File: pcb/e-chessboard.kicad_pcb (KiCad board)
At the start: 4 copper layers, 170 x 170 mm, 66 parts, among them J1 POWER, J2 UART, Q1 BC847, Q2 BC847, SW1 Reset, SW2 Boot, U1 ESP32-WROOM-32U, U10 MAGNET_LDR, U11 MAGNET_LDR, U12 MAGNET_LDR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

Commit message: feat(kicad): positioning power circuit and uart
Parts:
- U1: moved to B.Cu
- moved U1 247.4 mm to (229.5, 142.0), turned to 90 degrees
- moved R2 158.2 mm to (232.9, 166.5)
- moved R6 153.6 mm to (237.9, 170.0)
- moved R5 146.9 mm to (238.0, 163.5)
- moved U2 138.9 mm to (229.5, 100.5)
- moved C6 134.0 mm to (229.5, 94.5), turned to 180 degrees
- moved C8 129.2 mm to (231.5, 110.5), turned to 180 degrees
- moved F1 127.7 mm to (232.5, 120.0)
- moved D2 126.4 mm to (314.1, 201.1)
- moved D4 126.4 mm to (286.8, 233.5)
- moved D6 126.4 mm to (309.9, 201.1)
- moved D7 126.4 mm to (315.8, 196.8)
- moved R8 126.4 mm to (295.3, 216.8)
- moved C12 126.4 mm to (330.9, 175.5)
- moved C13 126.4 mm to (262.4, 244.6)
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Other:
- board size 170 x 170 mm -> 220 x 170 mm

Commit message: feat(kicad): placing all components
Placing all components to their places.
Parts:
- C3, C4, D1, D2, D4, D5, D6, D7: moved to B.Cu
- moved C14 279.9 mm to (53.0, 137.0), turned to 90 degrees
- moved R7 270.0 mm to (85.0, 66.5), turned to 270 degrees
- moved C15 261.6 mm to (67.0, 133.0), turned to 90 degrees
- moved R8 233.0 mm to (85.0, 116.5), turned to 270 degrees
- moved R9 198.3 mm to (85.0, 166.5), turned to 90 degrees
- moved C12 198.3 mm to (137.0, 217.0), turned to 180 degrees
- moved D9 197.7 mm to (110.0, 85.0), turned to 90 degrees
- moved D10 193.8 mm to (110.0, 135.0), turned to 90 degrees
- moved D11 184.6 mm to (110.0, 185.0), turned to 90 degrees
- moved D12 159.6 mm to (160.0, 85.0), turned to 90 degrees
- moved C13 136.0 mm to (133.0, 203.0), turned to 180 degrees
- moved U13 135.8 mm to (60.0, 135.0)
- moved D13 128.3 mm to (160.0, 135.0), turned to 90 degrees
- moved D14 127.1 mm to (160.2, 185.0), turned to 90 degrees
- moved C3 108.3 mm to (227.0, 128.8)
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
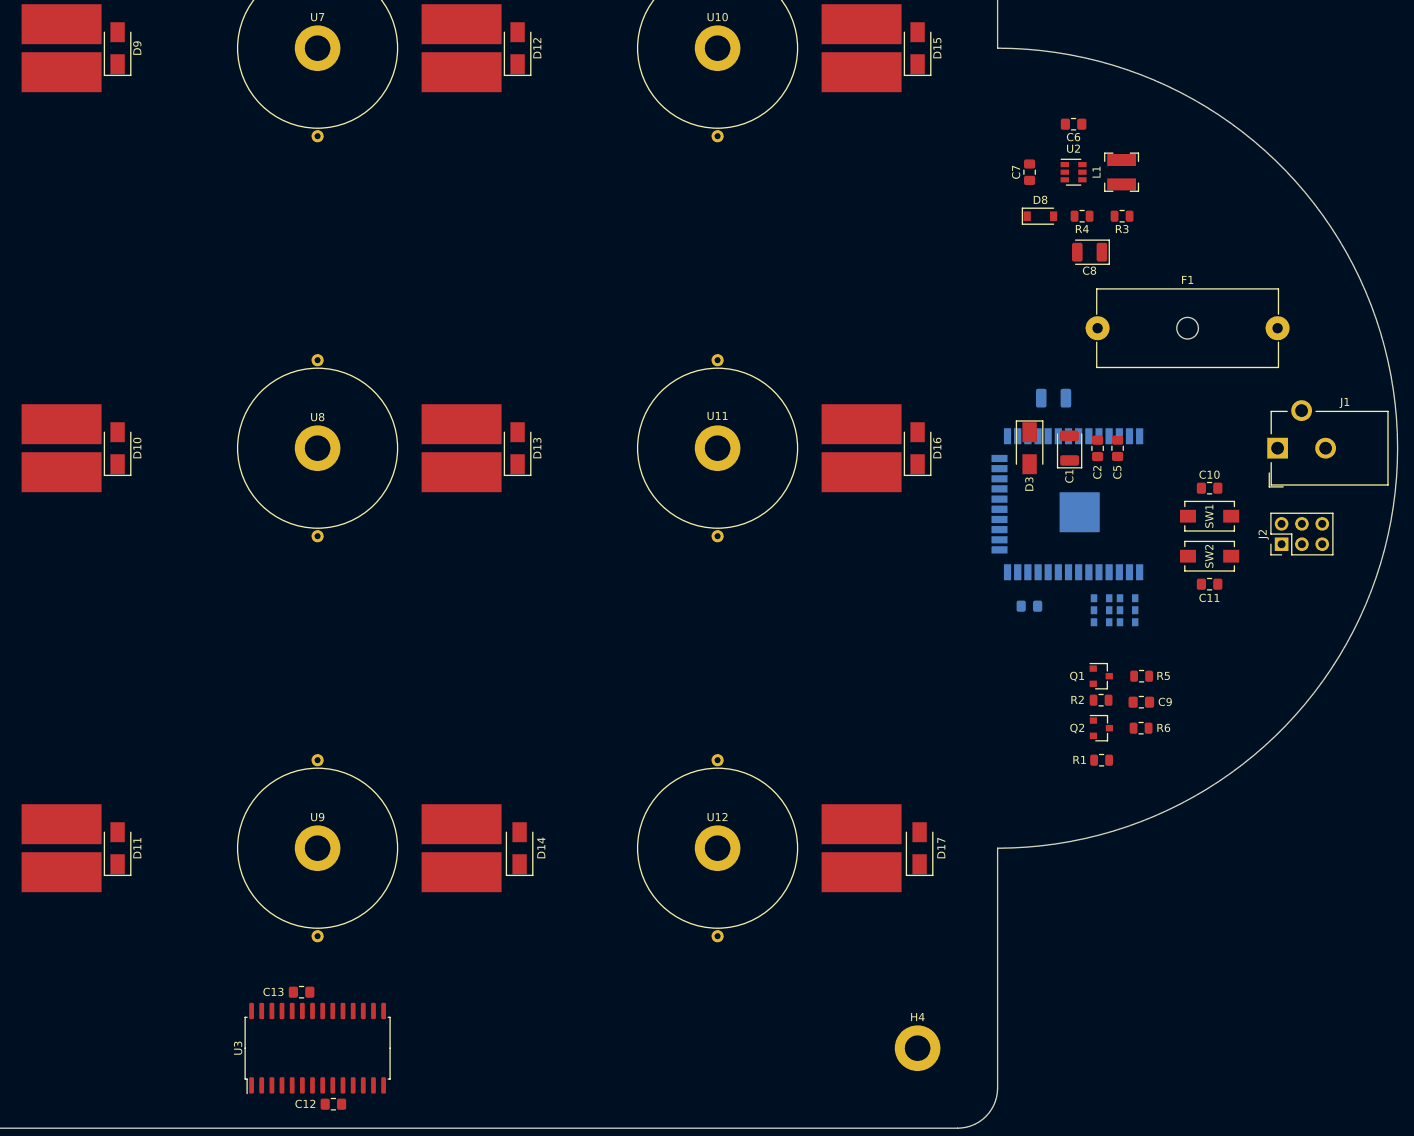
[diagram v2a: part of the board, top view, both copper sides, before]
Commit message: fix(kicad): redesign pcb
Removing outlayer to decrease the pcb size.
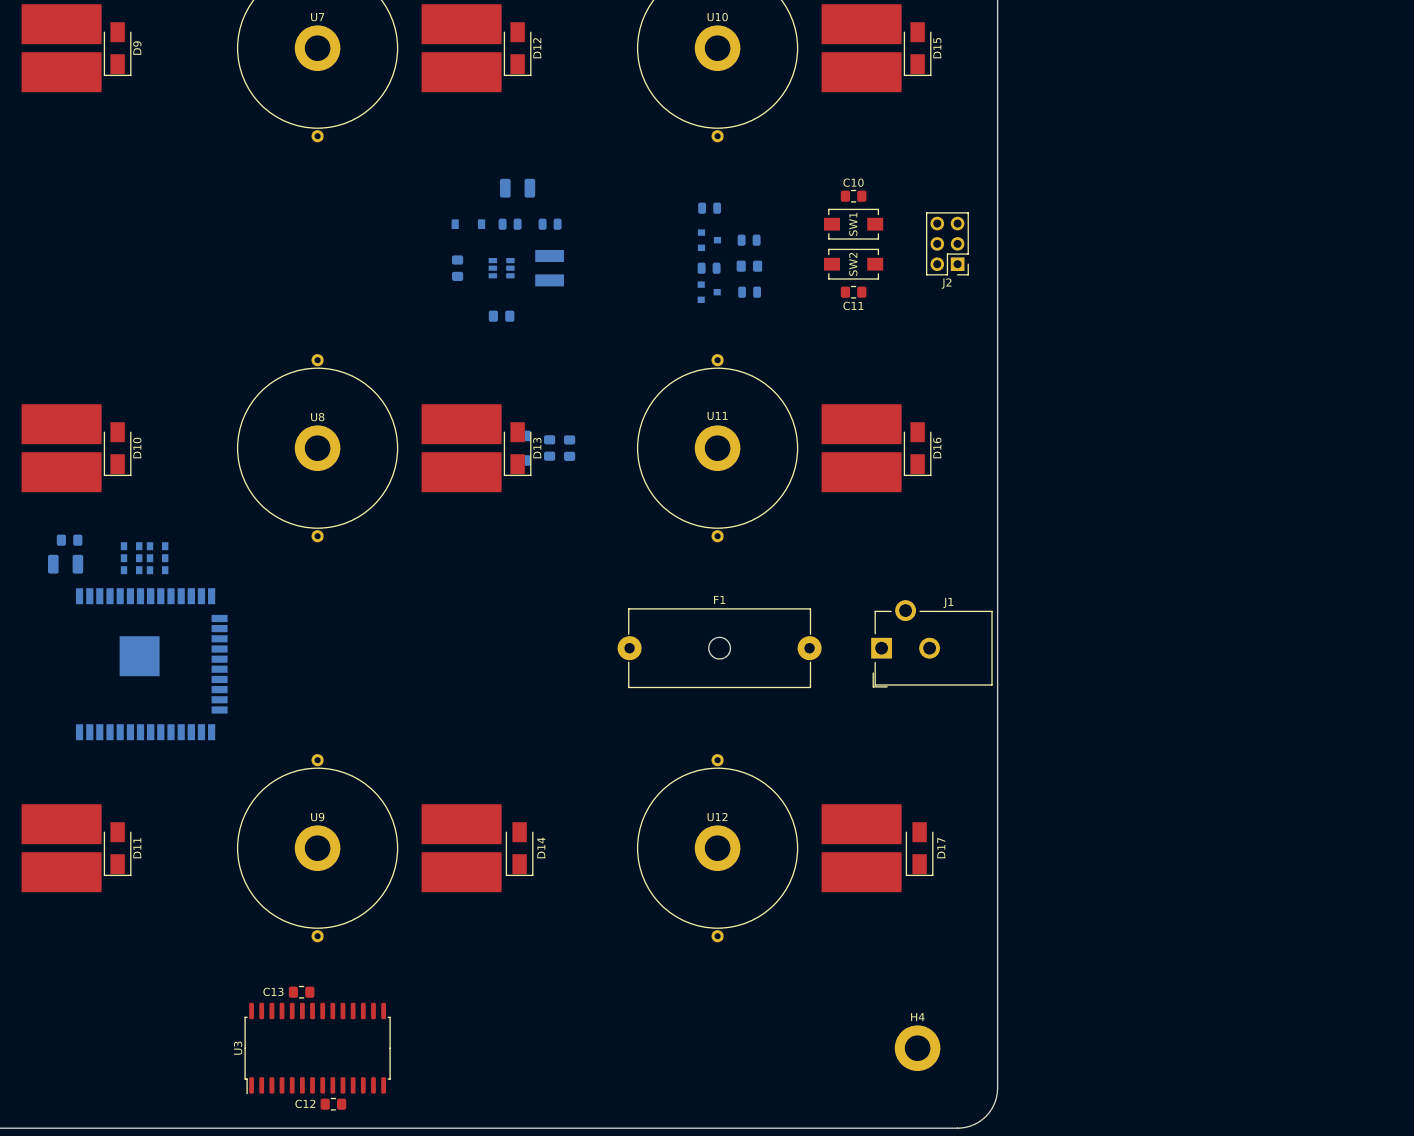
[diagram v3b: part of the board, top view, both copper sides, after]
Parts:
- C1, C2, C5, C6, C7, C8, C9, D3, D8, L1, Q1, Q2, R1, R2, R3, R4, R5, R6, U2: moved to B.Cu
- moved C3 125.2 mm to (103.5, 149.5), turned to 180 degrees
- moved D7 124.9 mm to (111.8, 147.2), turned to 180 degrees
- moved D5 124.7 mm to (111.8, 148.8), turned to 180 degrees
- moved D2 124.5 mm to (111.8, 150.2), turned to 180 degrees
- moved C4 120.3 mm to (104.0, 146.5)
- moved D6 118.4 mm to (115.0, 147.2), turned to 180 degrees
- moved D4 118.2 mm to (115.0, 148.8), turned to 180 degrees
- moved D1 118.1 mm to (115.0, 150.2), turned to 180 degrees
- moved U1 117.7 mm to (113.5, 162.0), turned to 270 degrees
- moved R1 84.6 mm to (184.0, 105.0)
- moved Q2 78.2 mm to (184.0, 109.0)
- moved R6 78.2 mm to (188.9, 109.0)
- moved C6 75.4 mm to (158.0, 118.5)
- moved C9 73.3 mm to (189.0, 112.2)
- moved R2 72.9 mm to (183.9, 112.5)
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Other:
- board size 220 x 170 mm -> 170 x 170 mm

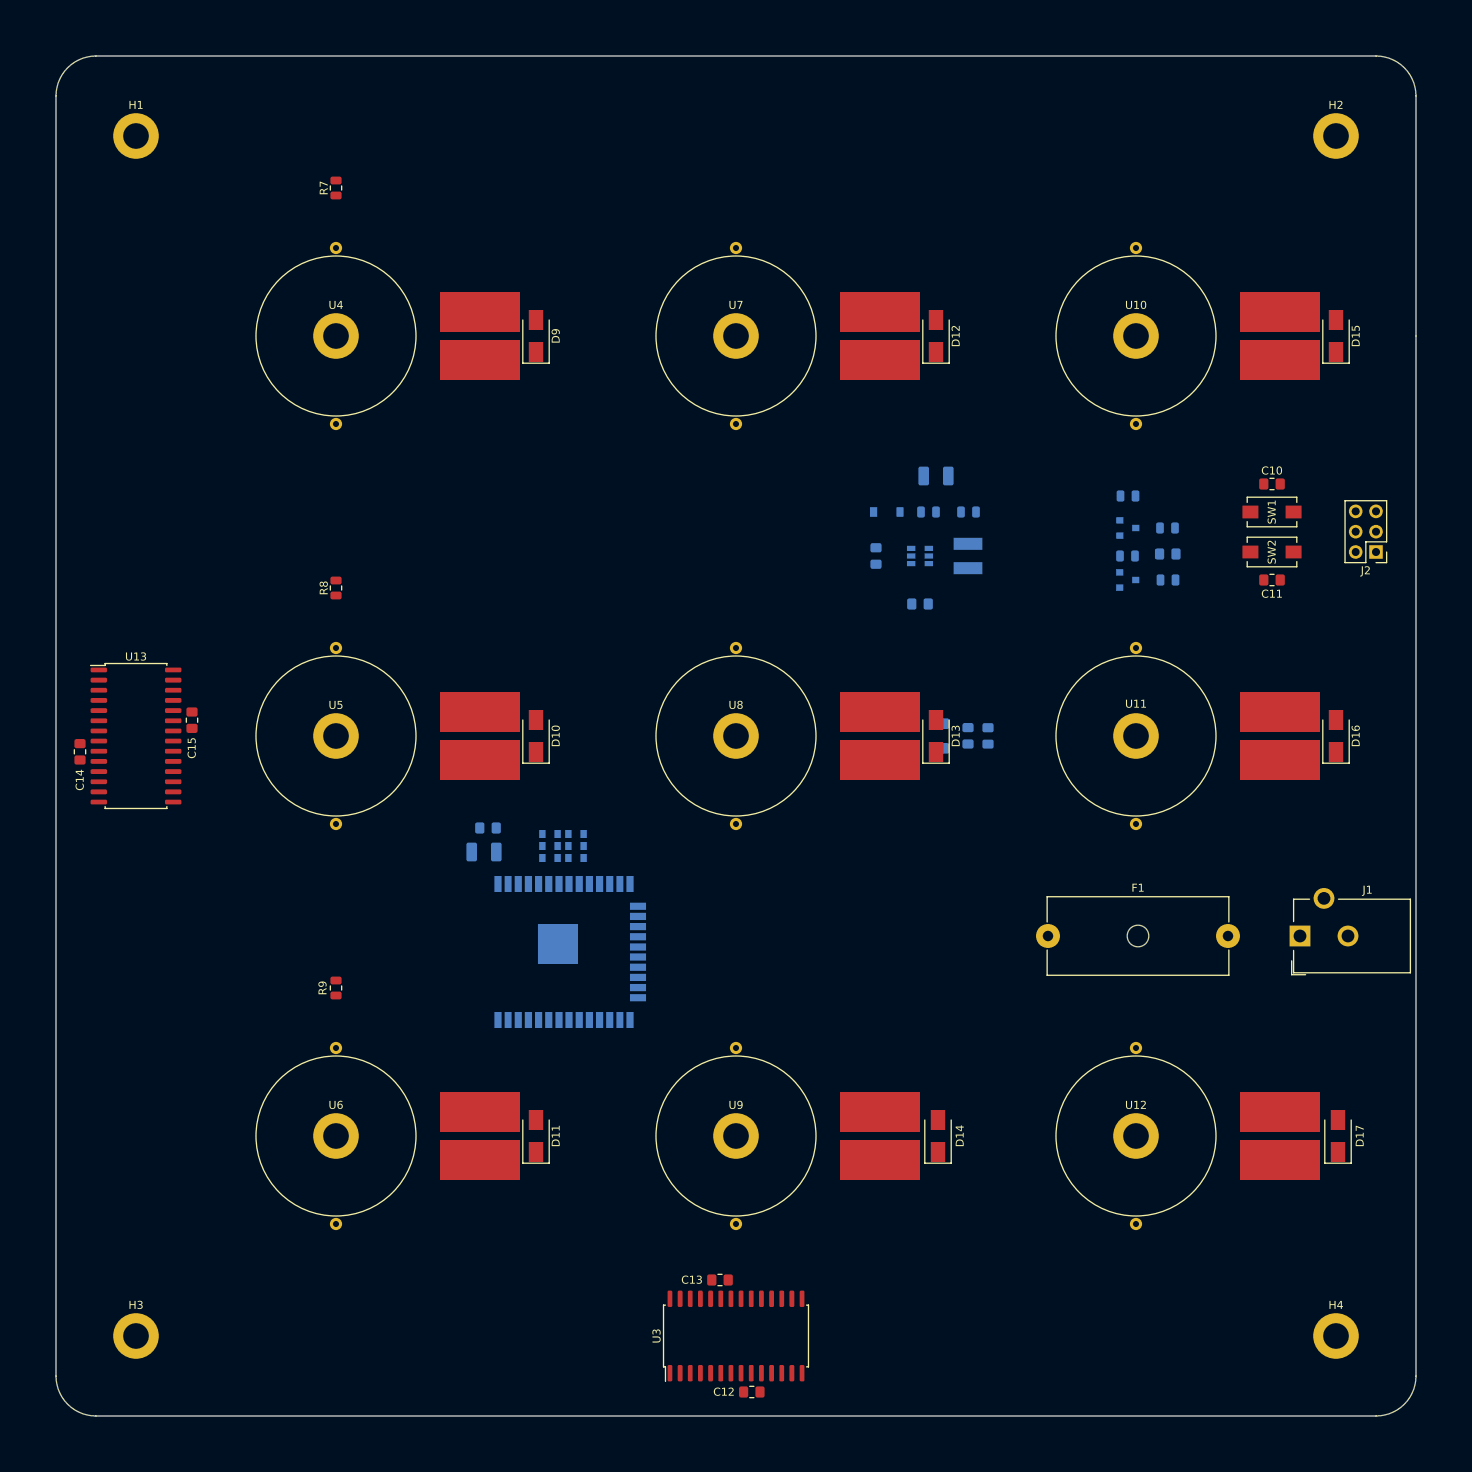
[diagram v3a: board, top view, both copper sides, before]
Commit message: fix(kicad): adding more traces
Adding traces and changing some schematic outputs for optimization.
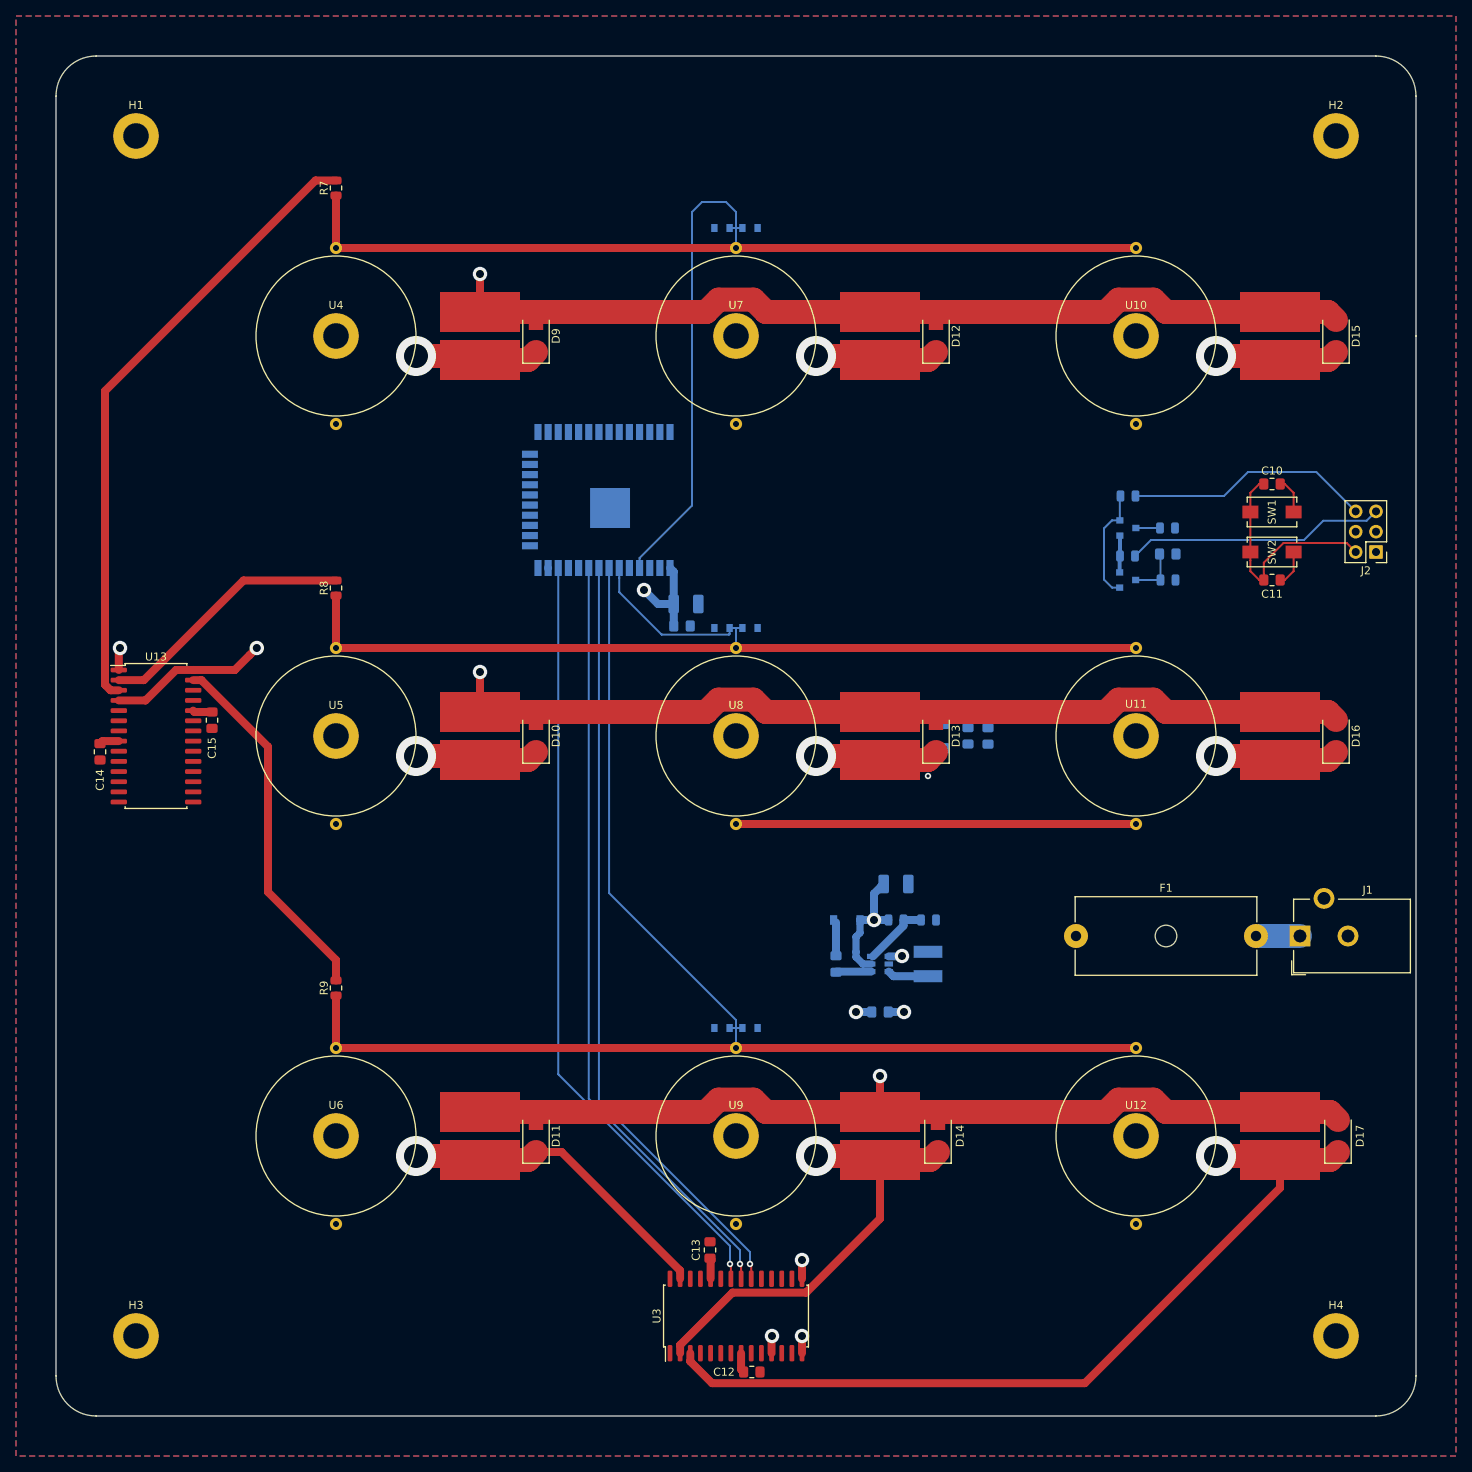
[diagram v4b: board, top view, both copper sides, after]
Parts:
- R7, R8, R9: value 10k -> 300k
- moved D1 81.7 mm to (136.8, 71.5)
- moved D2 81.6 mm to (133.2, 71.5)
- moved U1 56.7 mm to (118.5, 105.5), turned to 90 degrees
- moved C6 51.2 mm to (153.0, 169.5)
- moved C7 51.2 mm to (147.5, 163.5)
- moved C8 51.2 mm to (155.0, 153.5)
- moved D8 51.2 mm to (148.8, 158.0)
- moved L1 51.2 mm to (159.0, 163.5)
- moved R3 51.2 mm to (159.1, 158.0)
- moved U2 51.2 mm to (153.0, 163.5)
- moved R4 51.2 mm to (155.0, 158.0)
- moved C3 40.0 mm to (128.8, 118.5)
- moved C4 35.0 mm to (128.2, 121.2)
- moved D6 33.7 mm to (136.8, 121.5)
- moved D7 33.5 mm to (133.2, 121.5)
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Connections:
- D1 pad 2: LDR_ADC3 -> LDR_ADC1
- D10 pad 1: MAG_COL_1 -> MAG_COL_3
- D11 pad 1: MAG_COL_1 -> MAG_COL_3
- D15 pad 1: MAG_COL_3 -> MAG_COL_1
- D16 pad 1: MAG_COL_3 -> MAG_COL_1
- D17 pad 1: MAG_COL_3 -> MAG_COL_1
- D2 pad 1: LDR_ADC3 -> LDR_ADC1
- D4 pad 2: LDR_ADC2 -> LDR_ADC3
- D5 pad 1: LDR_ADC2 -> LDR_ADC3
- D6 pad 2: LDR_ADC1 -> LDR_ADC2
- D7 pad 1: LDR_ADC1 -> LDR_ADC2
- D9 pad 1: MAG_COL_1 -> MAG_COL_3
- U1 pad 12: MAG_PWM_ROW1 -> MAG_PWM_ROW3
- U1 pad 4: LDR_ADC3 -> LDR_ADC1
- U1 pad 6: LDR_ADC1 -> LDR_ADC2
- U1 pad 7: LDR_ADC2 -> LDR_ADC3
- U1 pad 8: MAG_PWM_ROW2 -> MAG_PWM_ROW1
- U1 pad 9: MAG_PWM_ROW3 -> MAG_PWM_ROW2
- U10 pad 2: MAG_COL_3 -> MAG_COL_1
- U11 pad 2: MAG_COL_3 -> MAG_COL_1
- U12 pad 2: MAG_COL_3 -> MAG_COL_1
- U4 pad 2: MAG_COL_1 -> MAG_COL_3
- U5 pad 2: MAG_COL_1 -> MAG_COL_3
- U6 pad 2: MAG_COL_1 -> MAG_COL_3
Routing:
- net MAG_ROW_1: track 0.00 -> 327.7 mm, vias 0 -> 2
- net MAG_COL_1: track 0.00 -> 236.6 mm, vias 0 -> 3
- net MAG_ROW_2: track 0.00 -> 233.1 mm, vias 0 -> 2
- net MAG_COL_2: track 0.00 -> 187.0 mm, vias 0 -> 4
- net LDR_ADC3: track 0.00 -> 174.7 mm
- net MAG_COL_3: track 0.00 -> 172.0 mm, vias 0 -> 3
- net MAG_ROW_3: track 0.00 -> 171.9 mm, vias 0 -> 2
- net LDR_ADC1: track 0.00 -> 166.4 mm
- net LDR_ADC2: track 0.00 -> 130.5 mm
- net GND: track 0.00 -> 110.7 mm, vias 0 -> 3
- net MAG_PWM_ROW3: track 0.00 -> 97.8 mm, vias 0 -> 1
- net MAG_PWM_ROW2: track 0.00 -> 96.7 mm, vias 0 -> 1
- net MAG_PWM_ROW1: track 0.00 -> 96.7 mm, vias 0 -> 1
- net LDR_ROW1: track 0.00 -> 78.5 mm
- net LDR_ROW3: track 0.00 -> 45.5 mm
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- added copper zone on In1.Cu, net +12V
- added copper zone on B.Cu, net +3V3
- added copper zone on F.Cu, net GND
- added copper zone on In2.Cu, net GND
